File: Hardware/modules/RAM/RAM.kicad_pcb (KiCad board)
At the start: 2 copper layers, 83.3 x 68.2 mm, 7 parts, among them J1 Bus_PCI_6502, U1 AS6C4008-55PCN, U2 CY62256-70PC

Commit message: Update Module Files and Readme
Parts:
- added G***: LOGO, Eigene:logo, F.Cu at (104.1, 106.0)
- added REF**: ESD-Logo_8.9x8mm_SilkScreen, Symbol:ESD-Logo_8.9x8mm_SilkScreen, F.Cu at (104.1, 116.8)
- added REF**: OSHW-Logo2_9.8x8mm_SilkScreen, Symbol:OSHW-Logo2_9.8x8mm_SilkScreen, F.Cu at (104.1, 126.4)
- added REF**: WEEE-Logo_5.6x8mm_SilkScreen, Symbol:WEEE-Logo_5.6x8mm_SilkScreen, F.Cu at (104.1, 135.9)
- added Ref**: Val**, Eigene:ladder_4, F.Cu at (97.2, 94.0)
- moved C1 2.59 mm to (134.6, 96.3)
- moved C2 2.59 mm to (159.5, 101.3)
- moved JP1 2.59 mm to (134.1, 117.3)
- moved U1 2.59 mm to (116.3, 96.3)
- moved U2 2.59 mm to (141.2, 101.3)
- moved JP2 2.09 mm to (159.0, 117.2)
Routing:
- net /A7: track 0.00 -> 99.1 mm, vias 0 -> 1
- net /A12: track 0.00 -> 98.9 mm, vias 0 -> 2
- net /A6: track 0.00 -> 97.6 mm, vias 0 -> 2
- net /A5: track 0.00 -> 95.6 mm, vias 0 -> 1
- net /A4: track 0.00 -> 94.2 mm, vias 0 -> 2
- net /A3: track 0.00 -> 91.7 mm, vias 0 -> 1
- net /A2: track 0.00 -> 90.2 mm, vias 0 -> 2
- net /A1: track 0.00 -> 88.2 mm, vias 0 -> 1
- net /A0: track 0.00 -> 86.8 mm, vias 0 -> 2
- net /A8: track 0.00 -> 82.0 mm, vias 0 -> 2
- net /RAM_3: track 0.00 -> 81.1 mm
- net /A13: track 0.00 -> 80.8 mm, vias 0 -> 1
- net /R/~{W}: track 0.00 -> 79.4 mm, vias 0 -> 1
- net /A9: track 0.00 -> 78.4 mm, vias 0 -> 1
- net /A11: track 0.00 -> 74.3 mm, vias 0 -> 1
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- added copper zone on In1.Cu, net +5V
- added copper zone on In2.Cu, net GND
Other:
- copper layers 2 -> 4
- board text added: "SY65 32k + 32x16k RAM"

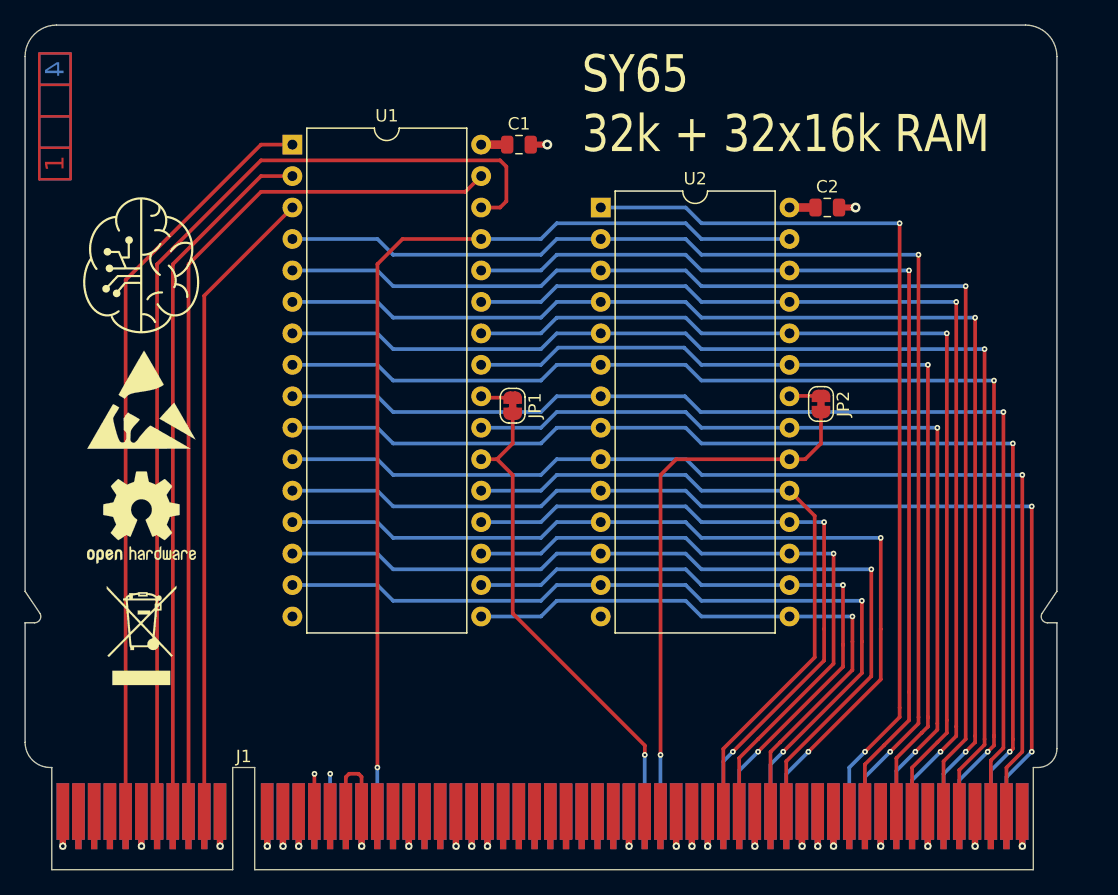
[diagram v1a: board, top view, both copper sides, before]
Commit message: Fix mirroring on High-Ram on Bank Select
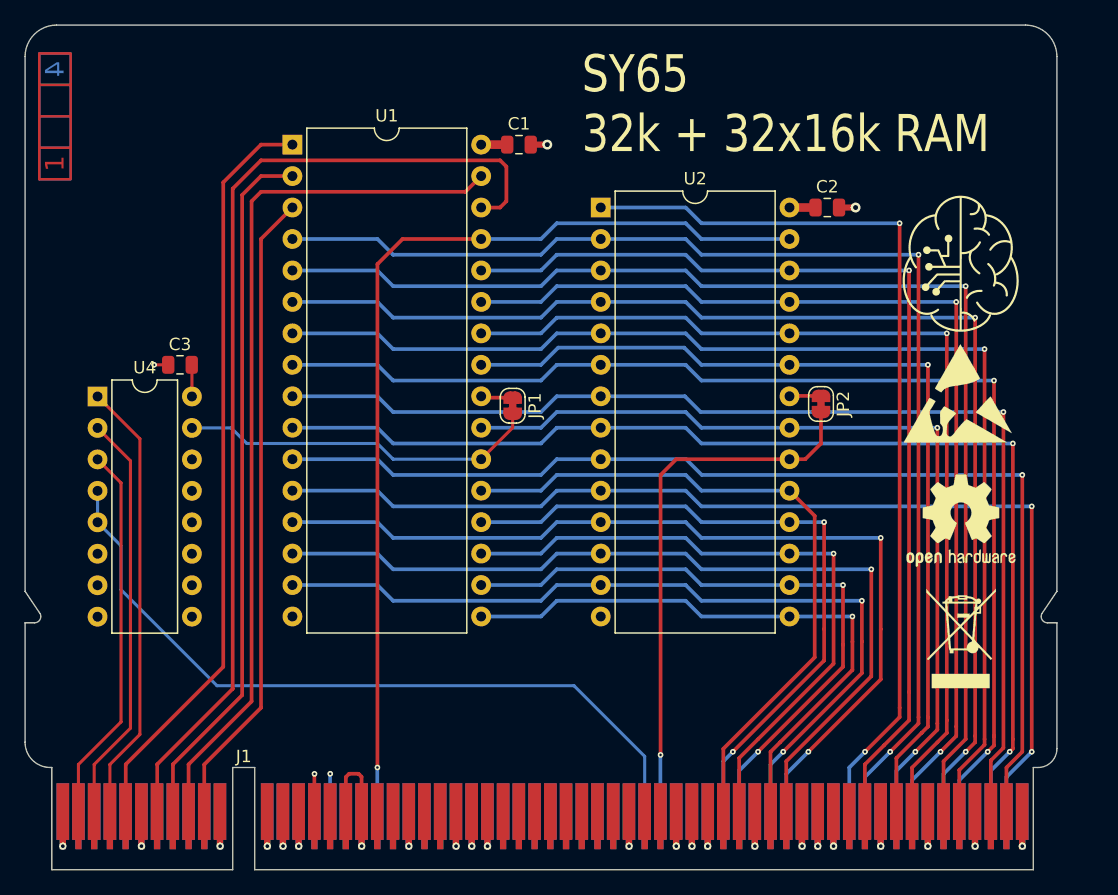
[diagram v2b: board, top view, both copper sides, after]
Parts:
- added C3: 100n, Capacitor_SMD:C_0805_2012Metric, F.Cu at (107.2, 114.0)
- added U4: 74HC138, Package_DIP:DIP-16_W7.62mm, F.Cu at (100.6, 116.6)
- moved REF** 66.2 mm to (170.3, 126.6)
- moved REF** 66.2 mm to (170.3, 136.1)
- moved G*** 66.2 mm to (170.3, 105.9)
- moved REF** 65.9 mm to (170.1, 116.3)
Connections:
- J1 pad A12: /A15 -> unconnected-(J1-A15-PadA12)_0
- J1 pad A24: /~{IO} -> unconnected-(J1-~{IO}-PadA24)_0
- J1 pad A25: /~{ROM} -> unconnected-(J1-~{ROM}-PadA25)_0
- J1 pad A27: /~{IRQ_0.0} -> unconnected-(J1-~{IRQ_0.0}-PadA27)_0
- J1 pad A28: /~{IRQ_0.1} -> unconnected-(J1-~{IRQ_0.1}-PadA28)
- J1 pad A29: /~{IRQ_0.2} -> unconnected-(J1-~{IRQ_0.2}-PadA29)
- J1 pad A30: /~{IRQ_0.3} -> unconnected-(J1-~{IRQ_0.3}-PadA30)_0
- J1 pad A31: /~{IRQ_0.4} -> unconnected-(J1-~{IRQ_0.4}-PadA31)
- J1 pad A32: /~{IRQ_0.5} -> unconnected-(J1-~{IRQ_0.5}-PadA32)
- J1 pad A33: /~{IRQ_0.6} -> unconnected-(J1-~{IRQ_0.6}-PadA33)
- J1 pad A34: /~{IRQ_0.7} -> unconnected-(J1-~{IRQ_0.7}-PadA34)_0
- J1 pad A38: /SYNC_VPA -> unconnected-(J1-Sync/VPA-PadA38)
- J1 pad A39: /Ø2/VDA -> unconnected-(J1-Ø2/VDA-PadA39)_0
- J1 pad A41: /~{RDY} -> unconnected-(J1-~{RDY}-PadA41)
- J1 pad A42: /~{BE} -> unconnected-(J1-~{BE}-PadA42)_0
- J1 pad A45: /E -> unconnected-(J1-E-PadA45)
- J1 pad B27: /~{IRQ} -> unconnected-(J1-~{IRQ}-PadB27)
- J1 pad B28: /~{IRQ_0} -> unconnected-(J1-~{IRQ_0}-PadB28)
- J1 pad B29: /~{IRQ_1} -> unconnected-(J1-~{IRQ_1}-PadB29)_0
- J1 pad B30: /~{IRQ_2} -> unconnected-(J1-~{IRQ_2}-PadB30)
- J1 pad B31: /~{IRQ_3} -> unconnected-(J1-~{IRQ_3}-PadB31)
- J1 pad B32: /~{IRQ_4} -> unconnected-(J1-~{IRQ_4}-PadB32)
- J1 pad B33: /~{NMI} -> unconnected-(J1-~{NMI}-PadB33)_0
- J1 pad B34: /PAGE -> unconnected-(J1-PAGE_ROM-PadB34)_0
- J1 pad B38: /~{VP} -> unconnected-(J1-~{VP}-PadB38)
- J1 pad B39: /~{ML} -> unconnected-(J1-~{ML}-PadB39)_0
- J1 pad B41: /~{RES} -> unconnected-(J1-~{RES}-PadB41)_0
- J1 pad B44: /CLK -> unconnected-(J1-CLK-PadB44)_0
- J1 pad B46: /M/X -> unconnected-(J1-M/~{X}-PadB46)_0
- J1 pad B53: /ROM_0 -> unconnected-(J1-ROM0-PadB53)_0
- J1 pad B54: /ROM_1 -> unconnected-(J1-ROM1-PadB54)
- J1 pad B55: /ROM_2 -> unconnected-(J1-ROM2-PadB55)
- J1 pad B56: /ROM_3 -> unconnected-(J1-ROM3-PadB56)
- J1 pad B58: /ROM_4 -> unconnected-(J1-ROM4-PadB58)_0
- J1 pad B59: /ROM_5 -> unconnected-(J1-ROM5-PadB59)_0
- J1 pad B60: /ROM_6 -> unconnected-(J1-ROM6-PadB60)
- J1 pad B61: /ROM_7 -> unconnected-(J1-ROM7-PadB61)
- JP1 pad 2: /~{H_RAM} -> Net-(JP1-B)
- U1 pad 22: /~{H_RAM} -> Net-(JP1-B)
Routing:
- net /RAM_5: track 0.00 -> 35.9 mm
- net /RAM_6: track 0.00 -> 33.3 mm
- net /RAM_7: track 0.00 -> 30.6 mm
- net Net-(JP1-B): track 0.00 -> 29.1 mm
- net /~{H_RAM}: track 38.9 -> 61.1 mm, vias 1 -> 0
- net +5V: track 4.20 -> 6.76 mm
- net GND: track 15.8 -> 17.0 mm, vias 22 -> 23

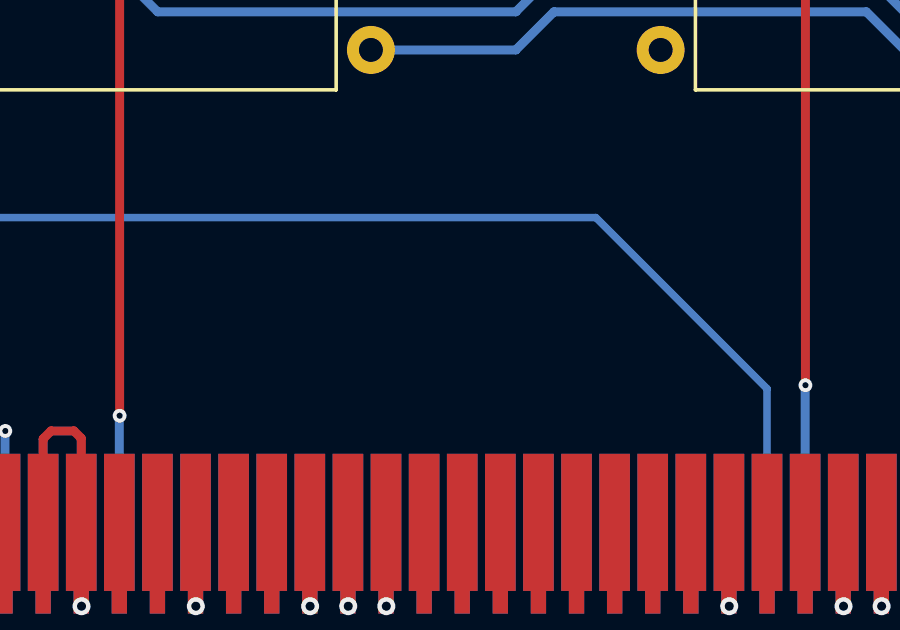
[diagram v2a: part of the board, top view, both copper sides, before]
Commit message: Hardware Review Pt. 1 fix Address Decoding for Strobe Generators add bulk capacitance to every board fix wiring of Prototyping Board
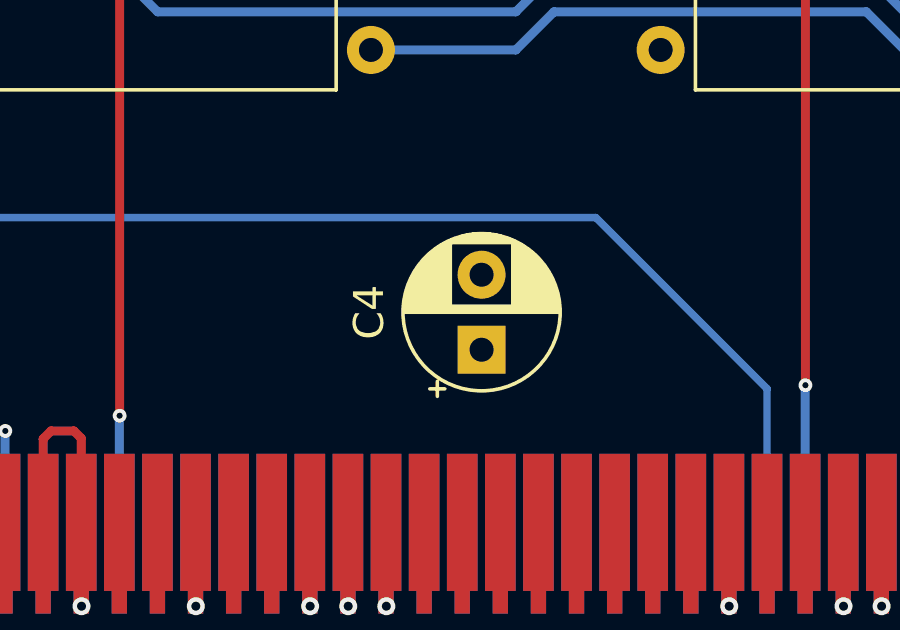
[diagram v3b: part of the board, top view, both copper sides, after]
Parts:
- added C4: 10µ, Capacitor_THT:CP_Radial_D5.0mm_P2.50mm, F.Cu at (135.3, 144.4)

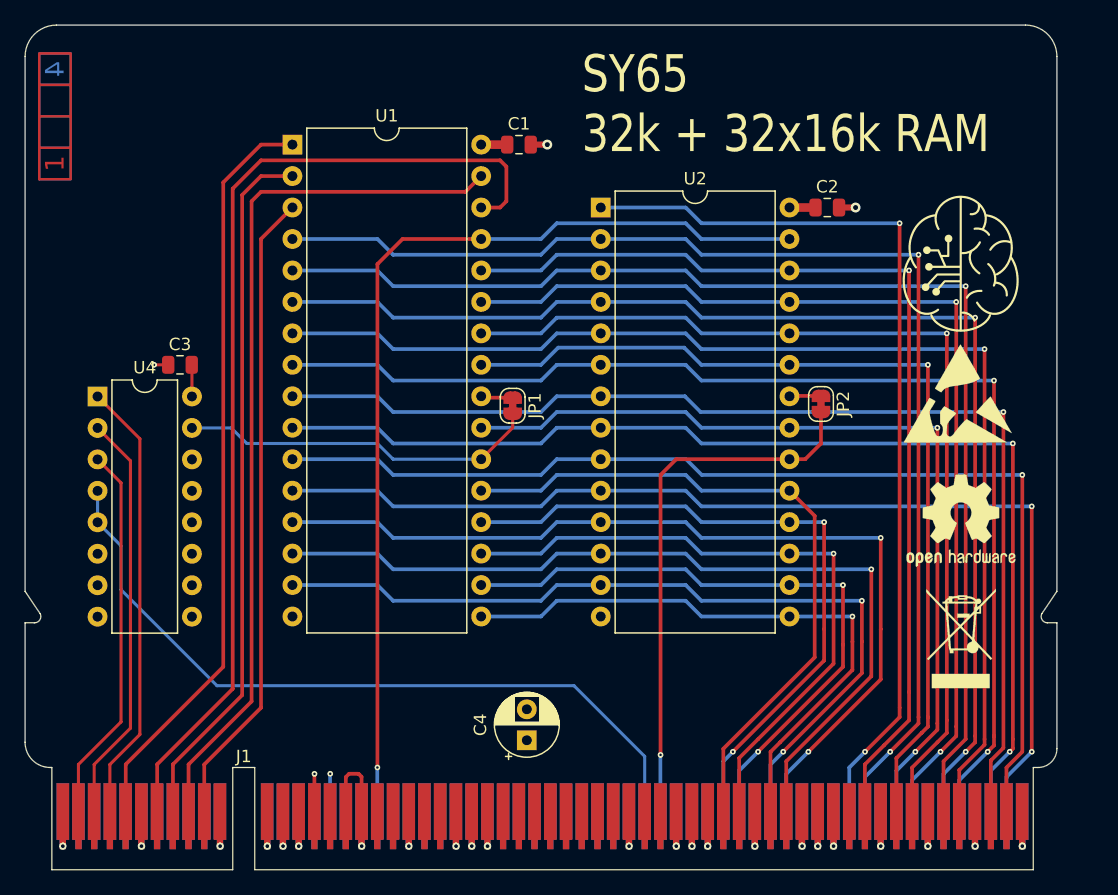
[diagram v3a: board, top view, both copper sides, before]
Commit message: Big Review Update - Changed Copper Pours on all PCBs - Implemented errors found at review - fixed some additional errors
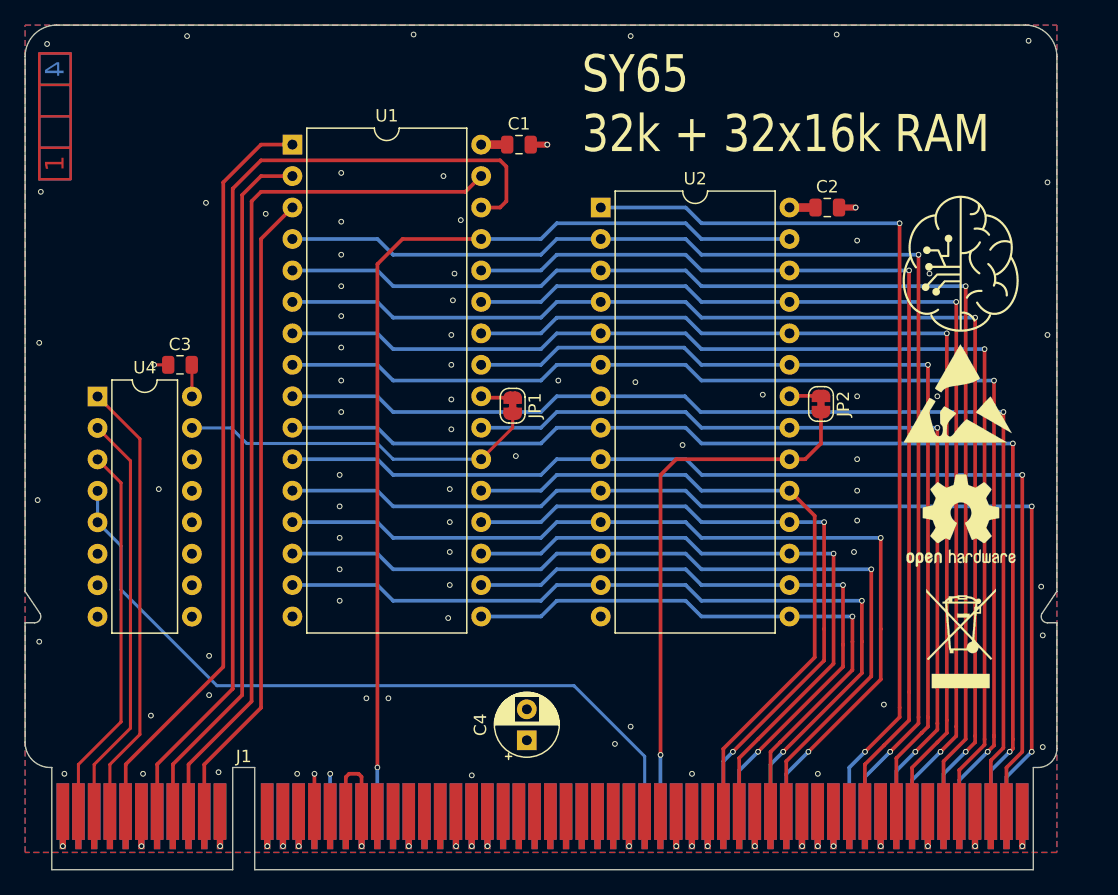
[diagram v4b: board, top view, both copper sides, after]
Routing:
- net +5V: vias 4 -> 76
- added copper zone on B.Cu, net +5V
- added copper zone on F.Cu, net +5V
- added copper zone on In1.Cu, net GND
- removed copper zone on In1.Cu, net +5V
